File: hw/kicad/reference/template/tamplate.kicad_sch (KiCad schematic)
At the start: 2 parts, among them J2 TOP, J4 BUTTOM

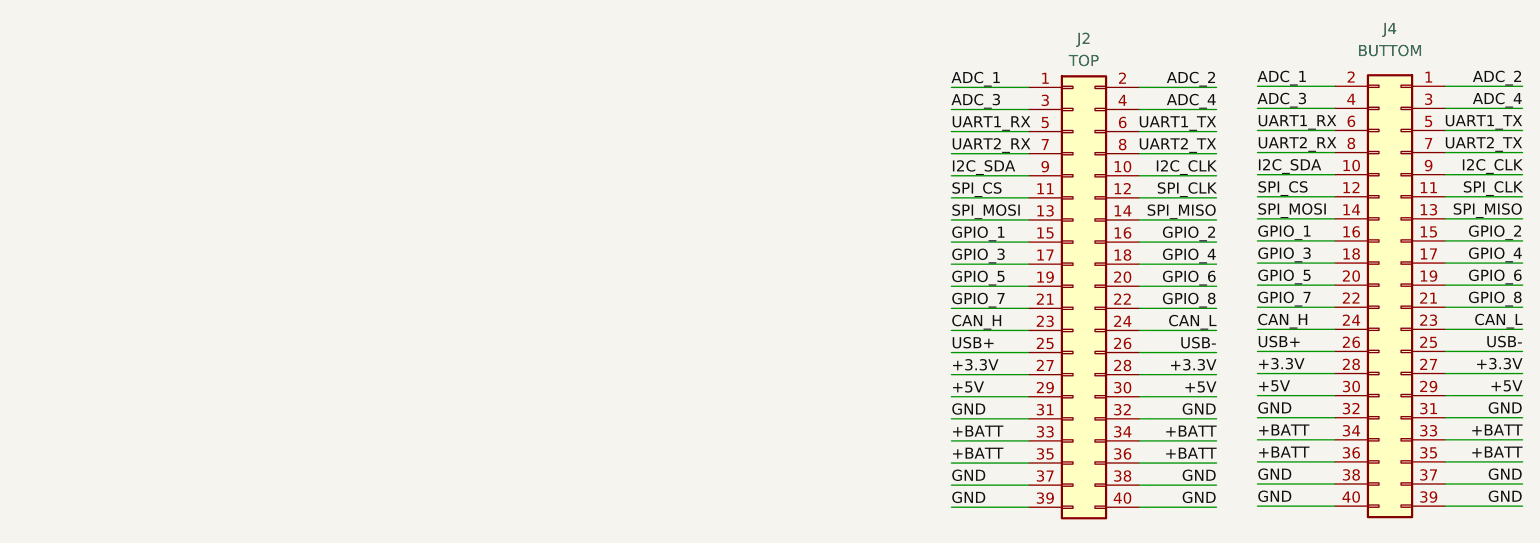
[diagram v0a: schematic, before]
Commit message: 更换接口线序
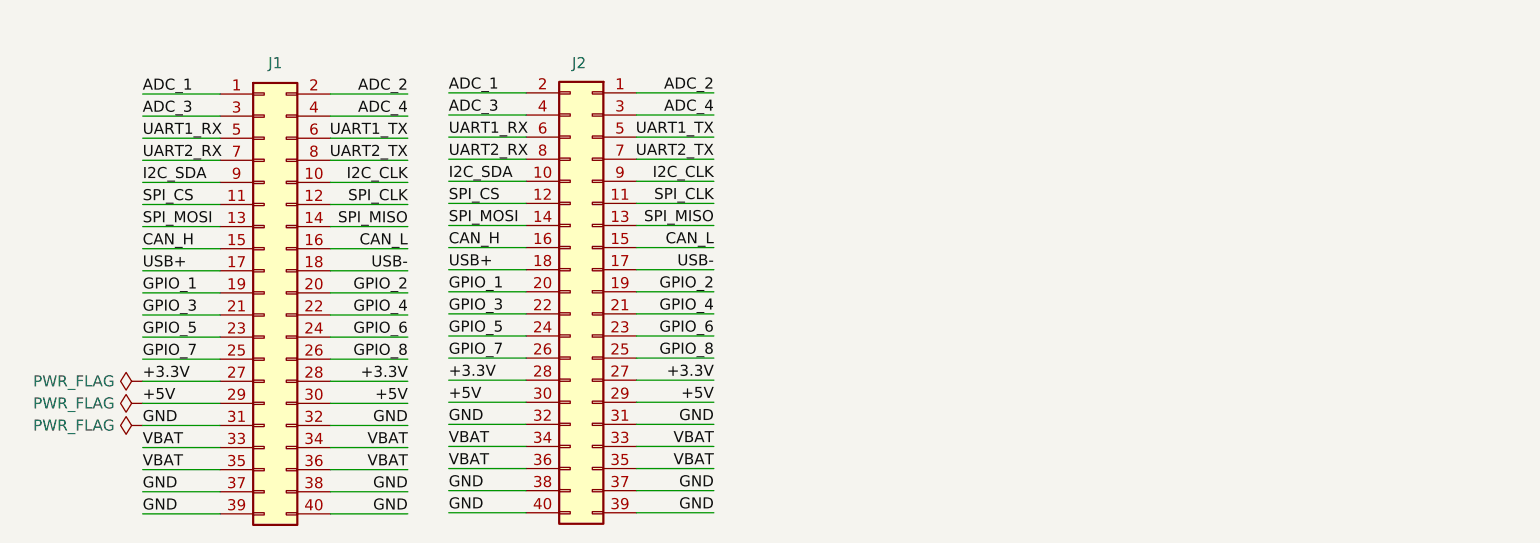
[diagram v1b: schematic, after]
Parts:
- removed J4: BUTTOM, Connector_PinHeader_1.27mm:PinHeader_2x20_P1.27mm_Vertical_SMD, symbol Connector_Generic:Conn_02x20_Odd_Even
- added J1: Conn_02x20_Odd_Even, Connector_PinHeader_1.27mm:PinHeader_2x20_P1.27mm_Vertical_SMD, symbol Connector_Generic:Conn_02x20_Odd_Even
- J2: value TOP -> Conn_02x20_Odd_Even
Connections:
- net +3.3V: now also J1.27 (Pin_27), J1.28 (Pin_28)
- net +5V: now also J1.29 (Pin_29), J1.30 (Pin_30)
- net ADC_1: now also J2.2 (Pin_2), J1.1 (Pin_1); no longer J2.1 (Pin_1)
- net ADC_2: now also J2.1 (Pin_1), J1.2 (Pin_2); no longer J2.2 (Pin_2)
- net ADC_3: now also J2.4 (Pin_4), J1.3 (Pin_3); no longer J2.3 (Pin_3)
- net ADC_4: now also J2.3 (Pin_3), J1.4 (Pin_4); no longer J2.4 (Pin_4)
- net CAN_H: now also J2.16 (Pin_16), J1.15 (Pin_15); no longer J2.23 (Pin_23)
- net CAN_L: now also J2.15 (Pin_15), J1.16 (Pin_16); no longer J2.24 (Pin_24)
- net GND: now also J1.31 (Pin_31), J1.32 (Pin_32), J1.37 (Pin_37), J1.38 (Pin_38), J1.39 (Pin_39), J1.40 (Pin_40)
- net GPIO_1: now also J2.20 (Pin_20), J1.19 (Pin_19); no longer J2.15 (Pin_15)
- net GPIO_2: now also J2.19 (Pin_19), J1.20 (Pin_20); no longer J2.16 (Pin_16)
- net GPIO_3: now also J2.22 (Pin_22), J1.21 (Pin_21); no longer J2.17 (Pin_17)
- net GPIO_4: now also J2.21 (Pin_21), J1.22 (Pin_22); no longer J2.18 (Pin_18)
- net GPIO_5: now also J2.24 (Pin_24), J1.23 (Pin_23); no longer J2.19 (Pin_19)
- net GPIO_6: now also J2.23 (Pin_23), J1.24 (Pin_24); no longer J2.20 (Pin_20)
- net GPIO_7: now also J2.26 (Pin_26), J1.25 (Pin_25); no longer J2.21 (Pin_21)
- net GPIO_8: now also J2.25 (Pin_25), J1.26 (Pin_26); no longer J2.22 (Pin_22)
- net I2C_CLK: now also J2.9 (Pin_9), J1.10 (Pin_10); no longer J2.10 (Pin_10)
- net I2C_SDA: now also J2.10 (Pin_10), J1.9 (Pin_9); no longer J2.9 (Pin_9)
- net SPI_CLK: now also J2.11 (Pin_11), J1.12 (Pin_12); no longer J2.12 (Pin_12)
- net SPI_CS: now also J2.12 (Pin_12), J1.11 (Pin_11); no longer J2.11 (Pin_11)
- net SPI_MISO: now also J2.13 (Pin_13), J1.14 (Pin_14); no longer J2.14 (Pin_14)
- net SPI_MOSI: now also J2.14 (Pin_14), J1.13 (Pin_13); no longer J2.13 (Pin_13)
- net UART1_RX: now also J2.6 (Pin_6), J1.5 (Pin_5); no longer J2.5 (Pin_5)
- net UART1_TX: now also J2.5 (Pin_5), J1.6 (Pin_6); no longer J2.6 (Pin_6)
- net UART2_RX: now also J2.8 (Pin_8), J1.7 (Pin_7); no longer J2.7 (Pin_7)
- net UART2_TX: now also J2.7 (Pin_7), J1.8 (Pin_8); no longer J2.8 (Pin_8)
- net USB+: now also J2.18 (Pin_18), J1.17 (Pin_17); no longer J2.25 (Pin_25)
- net USB-: now also J2.17 (Pin_17), J1.18 (Pin_18); no longer J2.26 (Pin_26)
- net +BATT renamed VBAT
- net VBAT: now also J1.33 (Pin_33), J1.34 (Pin_34), J1.35 (Pin_35), J1.36 (Pin_36)
